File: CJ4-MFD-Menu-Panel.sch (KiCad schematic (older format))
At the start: 50 parts, among them SW1 SW_Push_LED, SW10 5_Way_Switch, SW11 SW_Push_LED, SW12 SW_Push_LED, SW13 SW_Push_LED, SW14 SW_Push_LED, SW15 SW_Push_LED, SW16 SW_Push_LED, SW17 SW_Push_LED, SW18 SW_Push_LED, SW19 SW_Push_LED, SW2 SW_Push_LED, SW20 SW_Push_LED, SW21 SW_Push_LED, SW3 SW_Push_LED, SW4 SW_Push_LED, SW5 SW_Push_LED, SW6 SW_Push_LED, SW7 SW_Push_LED, SW8 SW_Push_LED, SW9 SW_Push_LED, U1 MCP23017_SO, U2 MCP23017_SO, U3 IS31FL3733B

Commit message: Layout + PCB
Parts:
- removed U1, U2: MCP23017_SO, Package_SO:SOIC-28W_7.5x17.9mm_P1.27mm, symbol Interface_Expansion:MCP23017_SO
- added J1: Conn_02x06_Counter_Clockwise, Connector_PinHeader_2.54mm:PinHeader_2x06_P2.54mm_Vertical, symbol Connector_Generic:Conn_02x06_Counter_Clockwise
- added U1, U2: MCP23017_ML, Package_DFN_QFN:QFN-28-1EP_6x6mm_P0.65mm_EP4.25x4.25mm, symbol Interface_Expansion:MCP23017_ML
- C1, C10, C11, C12, C13, C14, C15, C2, C3, C4, C5, C6, C7, C8, C9, R1, R10, R2, R3, R4, R5, R6, R7, R8, R9: footprint (none) -> CJ4-MFD-Menu-Panel:Perfect_0402
- ENC1: footprint ALPS-EC11EBB24C03-* -> CJ4-MFD-Menu-Panel:ALPS-EC11EBB24C03-0
- SW1, SW11, SW12, SW13, SW14, SW15, SW16, SW17, SW18, SW19, SW2, SW20, SW21, SW3, SW4, SW5, SW6, SW7, SW8, SW9: footprint (none) -> CJ4-MFD-Menu-Panel:SW_PUSH_6mm
- SW10: footprint (none) -> CJ4-MFD-Menu-Panel:5_Way_Switch
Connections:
- net +5V: now also J1.1 (Pin_1), U1.14 (~RESET~), U1.5 (VDD), U2.11 (A0), U2.14 (~RESET~), U2.5 (VDD)
- net A: now also ENC1.8 (A), R1.2, R8.1, J1.11 (Pin_11)
- net A': now also ENC1.1 (A'), R2.2, R7.1, J1.9 (Pin_9)
- net B: now also ENC1.10 (B), R3.2, R6.1, J1.10 (Pin_10)
- net B': now also ENC1.3 (B'), R4.2, R5.1, J1.8 (Pin_8)
- net CAS_PAGE: now also U2.25 (GPB0)
- net CHART: now also U1.21 (GPA4)
- net CKLIST: now also U2.27 (GPB2)
- net CRSR: now also U1.27 (GPB2)
- net CTR: now also U2.2 (GPB5)
- net DATABASE: now also U1.3 (GPB6)
- net DOWN: now also U2.17 (GPA0)
- net ENG: now also U1.28 (GPB3)
- net ESC: now also U1.1 (GPB4)
- net E_BTN: now also U2.18 (GPA1)
- net GND: now also SW1.1, SW11.1, SW12.1, SW13.1, SW14.1, SW15.1, SW16.1, SW17.1, SW18.1, SW19.1, SW2.1, SW20.1, SW21.1, SW3.1, SW4.1, SW5.1, SW6.1, SW7.1, SW8.1, SW9.1, J1.12 (Pin_12), U1.6 (VSS), U2.6 (VSS)
- net INTA_1: now also J1.4 (Pin_4), U1.16 (INTA)
- net INTA_2: now also J1.5 (Pin_5), U2.16 (INTA)
- net LED_INTB: now also J1.7 (Pin_7)
- net LEFT: now also U2.1 (GPB4)
- net LWR_MENU: now also U1.26 (GPB1)
- net MEM_1: now also U1.18 (GPA1)
- net MEM_2: now also U1.19 (GPA2)
- net MEM_3: now also U1.20 (GPA3)
- net NAV_DATA: now also U1.17 (GPA0)
- net PASS_BRIEF: now also U2.28 (GPB3)
- net RADAR_MENU: now also U1.22 (GPA5)
- net RIGHT: now also U2.4 (GPB7)
- net SCL: now also J1.3 (Pin_3), U1.8 (SCK), U2.8 (SCK)
- net SDA: now also J1.2 (Pin_2), U1.9 (SDA), U2.9 (SDA)
- net SDB: now also J1.6 (Pin_6)
- net SYS: now also U1.24 (GPA7)
- net TERR_WX: now also U1.2 (GPB5)
- net TFC: now also U1.4 (GPB7)
- net UP: now also U2.3 (GPB6)
- net UPR_MENU: now also U1.25 (GPB0)
- net ZOOM_MINUS: now also U1.23 (GPA6)
- net ZOOM_PLUS: now also U2.26 (GPB1)
- new net: U1.11 (A0), U1.12 (A1), U1.13 (A2), U1.29 (EP)
- new net: U2.12 (A1), U2.13 (A2), U2.29 (EP)
- no-connect marks 20 -> 26
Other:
- moved on the sheet: C1, C10, C11, C12, C13, C14, C15, C2, C3, C4, C5, C6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

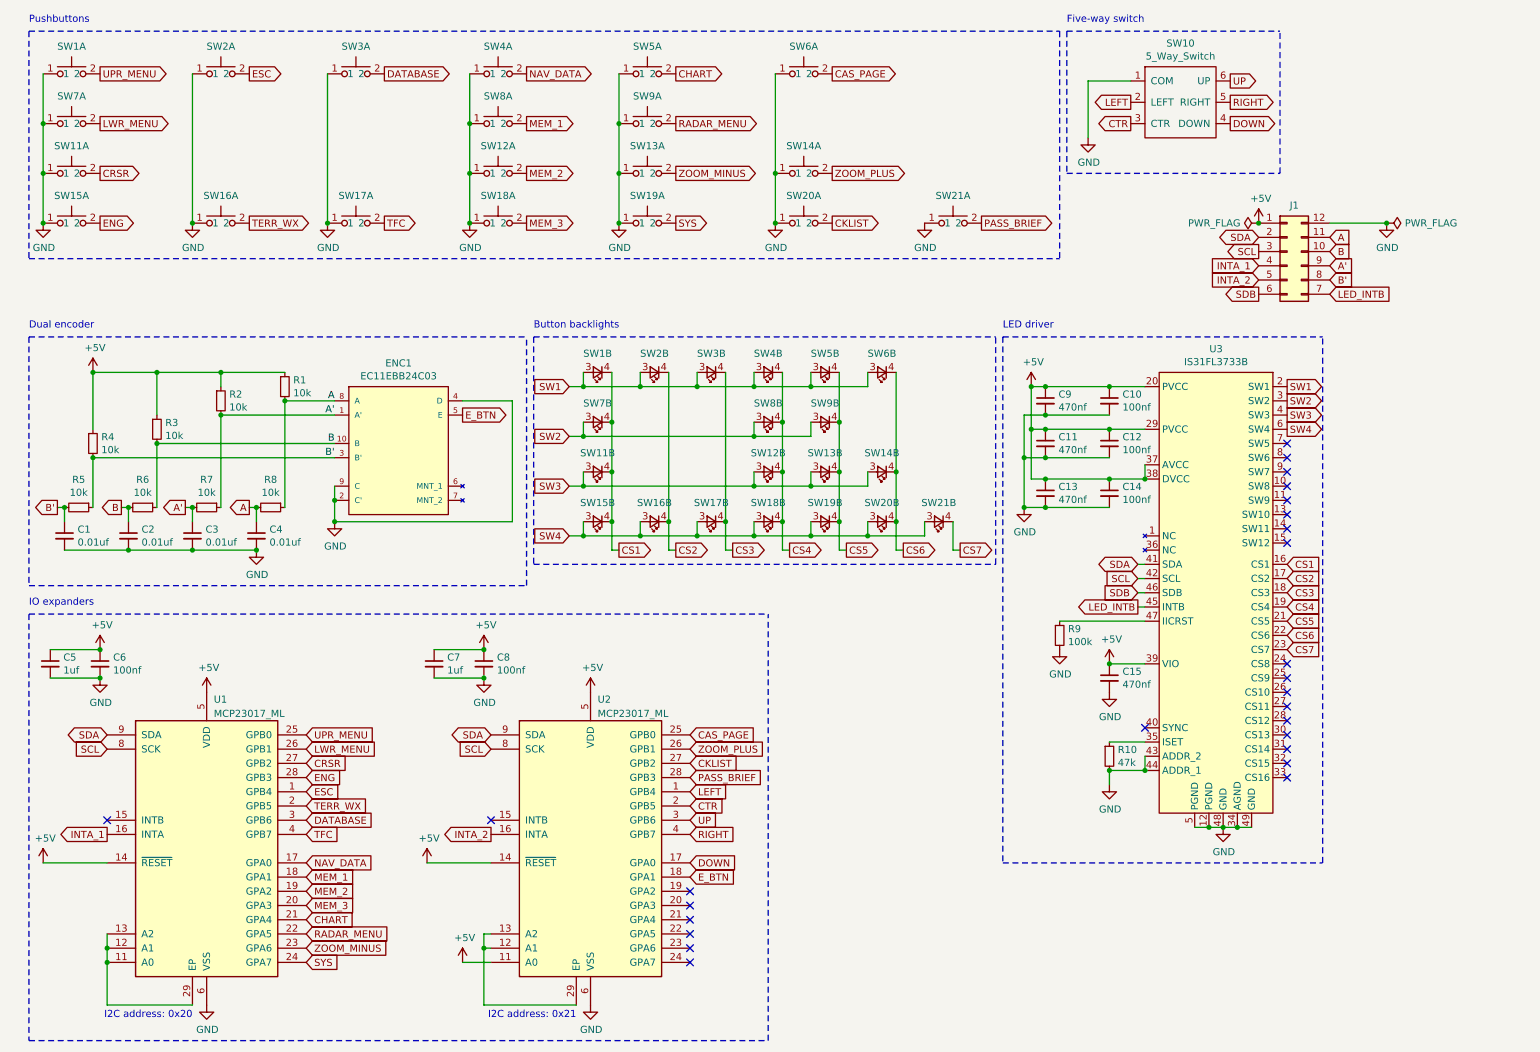
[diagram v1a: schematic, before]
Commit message: Switch footprint, attempt routing
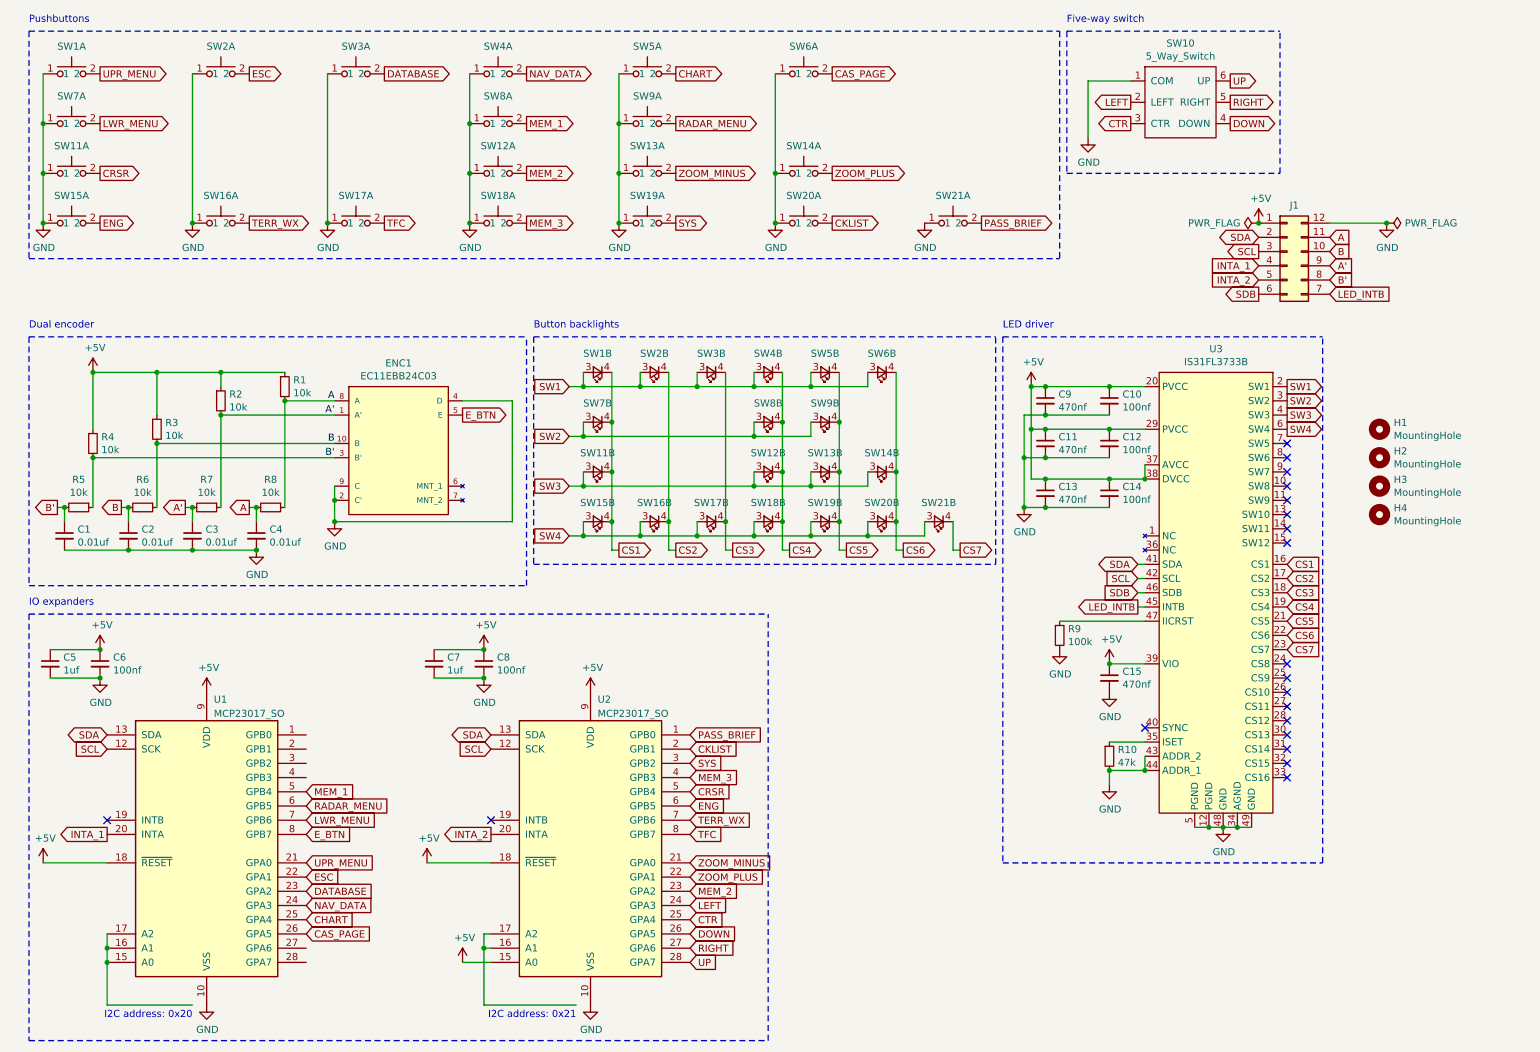
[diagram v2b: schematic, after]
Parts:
- removed U1, U2: MCP23017_ML, Package_DFN_QFN:QFN-28-1EP_6x6mm_P0.65mm_EP4.25x4.25mm, symbol Interface_Expansion:MCP23017_ML
- added H1, H2, H3, H4: MountingHole, MountingHole:MountingHole_3.2mm_M3, symbol Mechanical:MountingHole
- added U1, U2: MCP23017_SO, Package_SO:SOIC-28W_7.5x17.9mm_P1.27mm, symbol Interface_Expansion:MCP23017_SO
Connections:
- net +5V: now also U1.18 (~RESET~), U1.9 (VDD), U2.15 (A0), U2.18 (~RESET~), U2.9 (VDD)
- net CAS_PAGE: now also U1.26 (GPA5)
- net CHART: now also U1.25 (GPA4)
- net CKLIST: now also U2.2 (GPB1)
- net CRSR: now also U2.5 (GPB4)
- net CTR: now also U2.25 (GPA4)
- net DATABASE: now also U1.23 (GPA2)
- net DOWN: now also U2.26 (GPA5)
- net ENG: now also U2.6 (GPB5)
- net ESC: now also U1.22 (GPA1)
- net E_BTN: now also U1.8 (GPB7)
- net GND: now also U1.10 (VSS), U2.10 (VSS)
- net INTA_1: now also U1.20 (INTA)
- net INTA_2: now also U2.20 (INTA)
- net LEFT: now also U2.24 (GPA3)
- net LWR_MENU: now also U1.7 (GPB6)
- net MEM_1: now also U1.5 (GPB4)
- net MEM_2: now also U2.23 (GPA2)
- net MEM_3: now also U2.4 (GPB3)
- net NAV_DATA: now also U1.24 (GPA3)
- net PASS_BRIEF: now also U2.1 (GPB0)
- net RADAR_MENU: now also U1.6 (GPB5)
- net RIGHT: now also U2.27 (GPA6)
- net SCL: now also U1.12 (SCK), U2.12 (SCK)
- net SDA: now also U1.13 (SDA), U2.13 (SDA)
- net SYS: now also U2.3 (GPB2)
- net TERR_WX: now also U2.7 (GPB6)
- net TFC: now also U2.8 (GPB7)
- net UP: now also U2.28 (GPA7)
- net UPR_MENU: now also U1.21 (GPA0)
- net ZOOM_MINUS: now also U2.21 (GPA0)
- net ZOOM_PLUS: now also U2.22 (GPA1)
- new net: U1.15 (A0), U1.16 (A1), U1.17 (A2)
- new net: U2.16 (A1), U2.17 (A2)
- no-connect marks 26 -> 20
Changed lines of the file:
@@
 Text GLabel 7350 2000 2    50   Output ~ 0
 PASS_BRIEF
-Text GLabel 2600 5600 2    50   Input ~ 0
+Text GLabel 2600 6500 2    50   Input ~ 0
 UPR_MENU
-Text GLabel 2600 5700 2    50   Input ~ 0
+Text GLabel 2600 6200 2    50   Input ~ 0
 LWR_MENU
-Text GLabel 2600 5800 2    50   Input ~ 0
+Text GLabel 5300 6000 2    50   Input ~ 0
 CRSR
-Text GLabel 2600 5900 2    50   Input ~ 0
+Text GLabel 5300 6100 2    50   Input ~ 0
 ENG
+Text GLabel 2600 6600 2    50   Input ~ 0
+ESC
+Text GLabel 5300 6200 2    50   Input ~ 0
+TERR_WX
+Text GLabel 2600 6700 2    50   Input ~ 0
+DATABASE
+Text GLabel 5300 6300 2    50   Input ~ 0
+TFC
+Text GLabel 2600 6800 2    50   Input ~ 0
+NAV_DATA
 Text GLabel 2600 6000 2    50   Input ~ 0
-ESC
-Text GLabel 2600 6100 2    50   Input ~ 0
-TERR_WX
-Text GLabel 2600 6200 2    50   Input ~ 0
-DATABASE
-Text GLabel 2600 6300 2    50   Input ~ 0
-TFC
-Text GLabel 2600 6500 2    50   Input ~ 0
-NAV_DATA
-Text GLabel 2600 6600 2    50   Input ~ 0
 MEM_1
-Text GLabel 2600 6700 2    50   Input ~ 0
+Text GLabel 5300 6700 2    50   Input ~ 0
 MEM_2
-Text GLabel 2600 6800 2    50   Input ~ 0
+Text GLabel 5300 5900 2    50   Input ~ 0
 MEM_3
 Text GLabel 2600 6900 2    50   Input ~ 0
 CHART
-Text GLabel 2600 7000 2    50   Input ~ 0
+Text GLabel 2600 6100 2    50   Input ~ 0
 RADAR_MENU
-Text GLabel 2600 7100 2    50   Input ~ 0
+Text GLabel 5300 6500 2    50   Input ~ 0
 ZOOM_MINUS
-Text GLabel 2600 7200 2    50   Input ~ 0
+Text GLabel 5300 5800 2    50   Input ~ 0
 SYS
 $Comp
@@
 Wire Wire Line
 	3900 7200 3700 7200
+Text GLabel 2600 7000 2    50   Input ~ 0
+CAS_PAGE
+Text GLabel 5300 6600 2    50   Input ~ 0
+ZOOM_PLUS
+Text GLabel 5300 5700 2    50   Input ~ 0
+CKLIST
 Text GLabel 5300 5600 2    50   Input ~ 0
-CAS_PAGE
-Text GLabel 5300 5700 2    50   Input ~ 0
-ZOOM_PLUS
-Text GLabel 5300 5800 2    50   Input ~ 0
-CKLIST
-Text GLabel 5300 5900 2    50   Input ~ 0
 PASS_BRIEF
-Text GLabel 5300 6000 2    50   Input ~ 0
+Text GLabel 5300 6800 2    50   Input ~ 0
 LEFT
-Text GLabel 5300 6100 2    50   Input ~ 0
+Text GLabel 5300 6900 2    50   Input ~ 0
 CTR
-Text GLabel 5300 6200 2    50   Input ~ 0
+Text GLabel 5300 7200 2    50   Input ~ 0
 UP
-Text GLabel 5300 6300 2    50   Input ~ 0
+Text GLabel 5300 7100 2    50   Input ~ 0
 RIGHT
-Text GLabel 5300 6500 2    50   Input ~ 0
+Text GLabel 5300 7000 2    50   Input ~ 0
 DOWN
-Text GLabel 5300 6600 2    50   Input ~ 0
+Text GLabel 2600 6300 2    50   Input ~ 0
 E_BTN
 Text GLabel 8400 1150 0    50   Output ~ 0
@@
 Text GLabel 9800 2200 2    50   Input ~ 0
 B
-NoConn ~ 5300 6700
-NoConn ~ 5300 6800
-NoConn ~ 5300 6900
-NoConn ~ 5300 7000
-NoConn ~ 5300 7100
-NoConn ~ 5300 7200
 Wire Wire Line
 	2800 3850 2800 3950
@@
 	1    0    0    -1
 $EndComp
-Wire Wire Line
-	1200 7000 1200 7100
-$Comp
-L Interface_Expansion:MCP23017_ML U1
-U 1 1 61BAE6AC
-P 1900 6400
-F 0 "U1" H 1950 7450 50  0000 L CNN
-F 1 "MCP23017_ML" H 1950 7350 50  0000 L CNN
-F 2 "Package_DFN_QFN:QFN-28-1EP_6x6mm_P0.65mm_EP4.25x4.25mm" H 2100 5400 50  0001 L CNN
-F 3 "http://ww1.microchip.com/downloads/en/DeviceDoc/20001952C.pdf" H 2100 5300 50  0001 L CNN
-	1    1900 6400
-	1    0    0    -1
-$EndComp
-Wire Wire Line
-	1200 7200 1200 7500
-$Comp
-L Interface_Expansion:MCP23017_ML U2
-U 1 1 61BAFEB9
-P 4600 6400
-F 0 "U2" H 4650 7450 50  0000 L CNN
-F 1 "MCP23017_ML" H 4650 7350 50  0000 L CNN
-F 2 "Package_DFN_QFN:QFN-28-1EP_6x6mm_P0.65mm_EP4.25x4.25mm" H 4800 5400 50  0001 L CNN
-F 3 "http://ww1.microchip.com/downloads/en/DeviceDoc/20001952C.pdf" H 4800 5300 50  0001 L CNN
-	1    4600 6400
-	1    0    0    -1
-$EndComp
 $Comp
 L Connector_Generic:Conn_02x06_Counter_Clockwise J1
@@
 Connection ~ 2800 4100
 Wire Wire Line
+	1200 7000 1200 7100
+$Comp
+L Interface_Expansion:MCP23017_SO U1
+U 1 1 61A8CC7A
+P 1900 6400
+F 0 "U1" H 1950 7450 50  0000 L CNN
+F 1 "MCP23017_SO" H 1950 7350 50  0000 L CNN
+F 2 "Package_SO:SOIC-28W_7.5x17.9mm_P1.27mm" H 2100 5400 50  0001 L CNN
+F 3 "http://ww1.microchip.com/downloads/en/DeviceDoc/20001952C.pdf" H 2100 5300 50  0001 L CNN
+	1    1900 6400
+	1    0    0    -1
+$EndComp
+Wire Wire Line
+	1200 7200 1200 7500
+$Comp
+L Interface_Expansion:MCP23017_SO U2
+U 1 1 61A8E2E8
+P 4600 6400
+F 0 "U2" H 4650 7450 50  0000 L CNN
+F 1 "MCP23017_SO" H 4650 7350 50  0000 L CNN
+F 2 "Package_SO:SOIC-28W_7.5x17.9mm_P1.27mm" H 4800 5400 50  0001 L CNN
+F 3 "http://ww1.microchip.com/downloads/en/DeviceDoc/20001952C.pdf" H 4800 5300 50  0001 L CNN
+	1    4600 6400
+	1    0    0    -1
+$EndComp
+Wire Wire Line
 	1200 7200 1200 7100
 Connection ~ 1200 7200
 Connection ~ 1200 7100
+$Comp
+L Mechanical:MountingHole H1
+U 1 1 61C86547
+P 10150 3450
+F 0 "H1" H 10250 3496 50  0000 L CNN
+F 1 "MountingHole" H 10250 3405 50  0000 L CNN
+F 2 "MountingHole:MountingHole_3.2mm_M3" H 10150 3450 50  0001 C CNN
+F 3 "~" H 10150 3450 50  0001 C CNN
+	1    10150 3450
+	1    0    0    -1
+$EndComp
+$Comp
+L Mechanical:MountingHole H2
+U 1 1 61C86FDA
+P 10150 3650
+F 0 "H2" H 10250 3696 50  0000 L CNN
+F 1 "MountingHole" H 10250 3605 50  0000 L CNN
+F 2 "MountingHole:MountingHole_3.2mm_M3" H 10150 3650 50  0001 C CNN
+F 3 "~" H 10150 3650 50  0001 C CNN
+	1    10150 3650
+	1    0    0    -1
+$EndComp
+$Comp
+L Mechanical:MountingHole H3
+U 1 1 61C8D6E0
+P 10150 3850
+F 0 "H3" H 10250 3896 50  0000 L CNN
+F 1 "MountingHole" H 10250 3805 50  0000 L CNN
+F 2 "MountingHole:MountingHole_3.2mm_M3" H 10150 3850 50  0001 C CNN
+F 3 "~" H 10150 3850 50  0001 C CNN
+	1    10150 3850
+	1    0    0    -1
+$EndComp
+$Comp
+L Mechanical:MountingHole H4
+U 1 1 61C93C97
+P 10150 4050
+F 0 "H4" H 10250 4096 50  0000 L CNN
+F 1 "MountingHole" H 10250 4005 50  0000 L CNN
+F 2 "MountingHole:MountingHole_3.2mm_M3" H 10150 4050 50  0001 C CNN
+F 3 "~" H 10150 4050 50  0001 C CNN
+	1    10150 4050
+	1    0    0    -1
+$EndComp
 $EndSCHEMATC

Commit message: Footprint changes, update board size
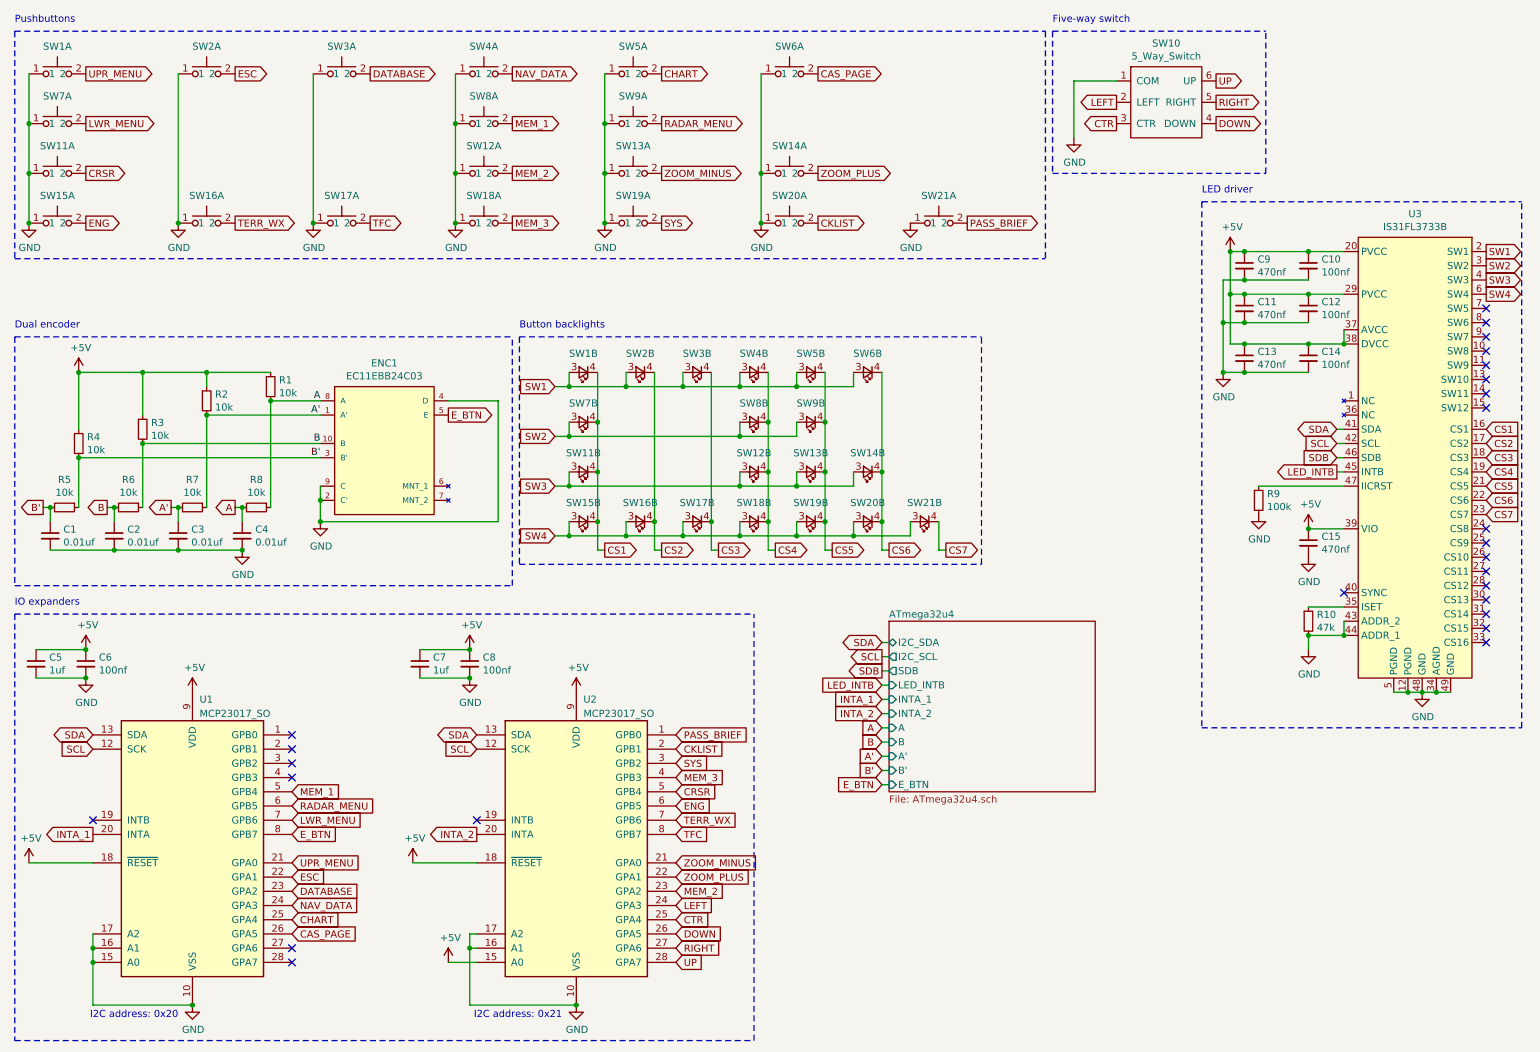
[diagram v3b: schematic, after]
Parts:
- removed H1, H2, H3, H4: MountingHole, MountingHole:MountingHole_3.2mm_M3, symbol Mechanical:MountingHole
- removed J1: Conn_02x06_Counter_Clockwise, Connector_PinHeader_2.54mm:PinHeader_2x06_P2.54mm_Vertical, symbol Connector_Generic:Conn_02x06_Counter_Clockwise
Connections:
- net GND: now also U1.15 (A0), U1.16 (A1), U1.17 (A2), U2.16 (A1), U2.17 (A2)
- no-connect marks 20 -> 26
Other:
- moved on the sheet: C1, C10, C11, C12, C13, C14, C15, C2, C3, C4, C5, C6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

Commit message: More routing. What a pain.
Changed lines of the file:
@@
 	8900 1850 8900 5550
-Wire Notes Line
-	8900 5550 11150 5550
 Wire Notes Line
 	11150 5550 11150 1850
@@
 F10 "A'" I L 6700 5750 50
 F11 "B'" I L 6700 5850 50
-F12 "E_BTN" I L 6700 5950 50
 $EndSheet
 Wire Wire Line
@@
 Wire Wire Line
 	6700 5850 6650 5850
-Wire Wire Line
-	6700 5950 6650 5950
 Text GLabel 6650 5550 0    50   Input ~ 0
 A
@@
 Text GLabel 6650 5850 0    50   Input ~ 0
 B'
-Text GLabel 6650 5950 0    50   Input ~ 0
-E_BTN
+Wire Notes Line
+	8900 5550 11150 5550
 $EndSCHEMATC
